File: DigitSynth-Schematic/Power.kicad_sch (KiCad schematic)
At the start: 0 parts

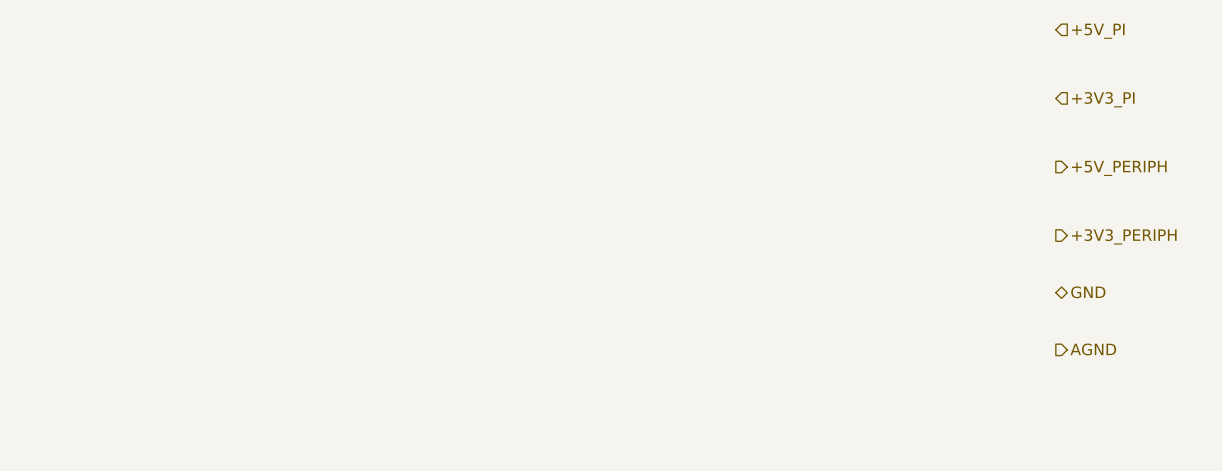
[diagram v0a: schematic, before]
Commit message: Add completed KiCad schematic hierarchy (Pi interface, ADC, LEDs, buttons, power)
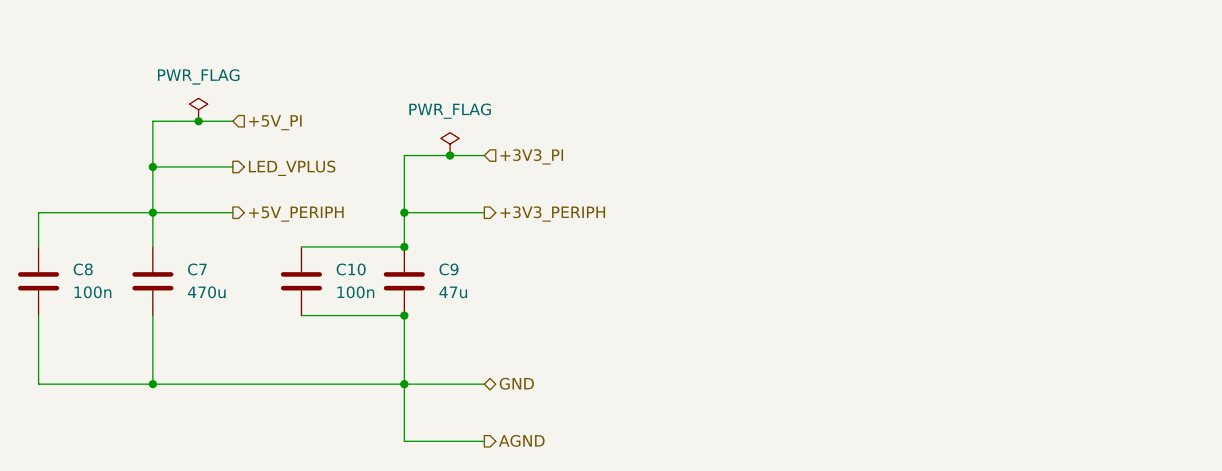
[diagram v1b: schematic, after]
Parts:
- added C10, C8: 100n, symbol Device:C
- added C7: 470u, symbol Device:C
- added C9: 47u, symbol Device:C
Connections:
- net +3V3_PERIPH: now also C10.1, C9.1
- net +5V_PERIPH: now also C7.1, C8.1
- net AGND: now also C10.2, C7.2, C8.2, C9.2
